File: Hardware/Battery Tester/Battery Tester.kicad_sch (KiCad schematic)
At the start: 16 parts, among them J1 USB4105-GF-A, J2 Conn_01x02_Socket, SW1 SW_SPST, U1 MCP73831-5-OT, U2 LP5907MFX-3.3_NOPB

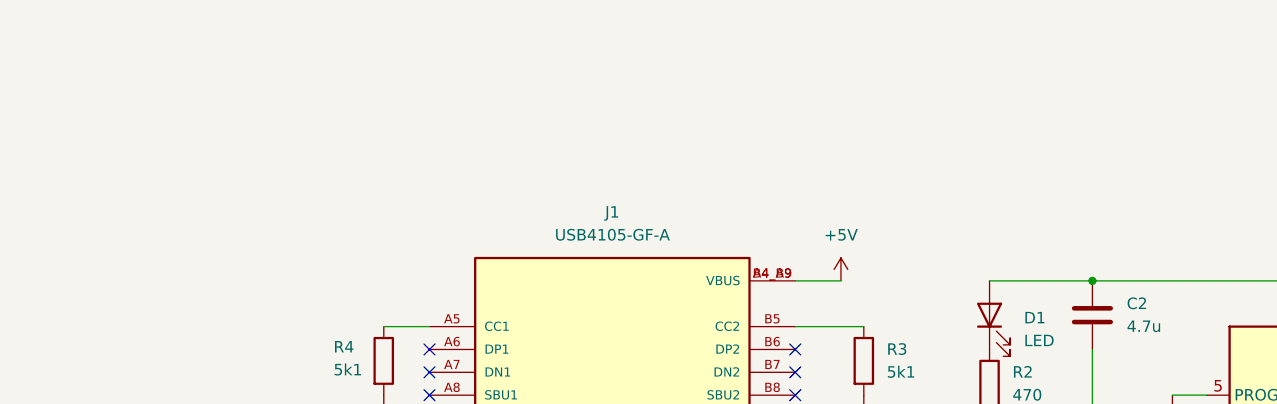
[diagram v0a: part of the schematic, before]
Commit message: Adding PDFs for the schematics
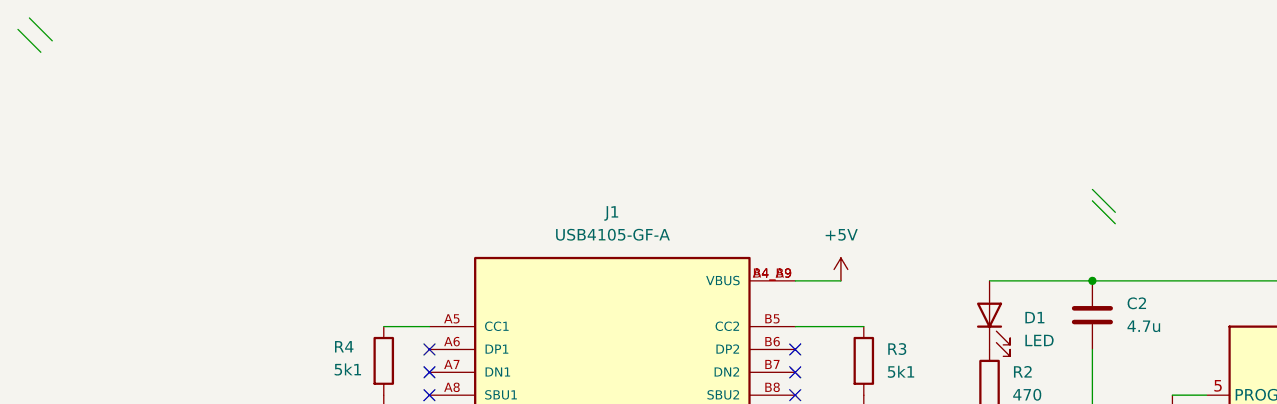
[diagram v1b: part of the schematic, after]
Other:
- title: (none) -> Battery Tester
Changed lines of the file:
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@@
 	(generator_version "8.0")
 	(paper "A4")
+	(title_block
+		(title "Battery Tester")
+		(date "2024-04-16")
+		(rev "Rev A")
+	)
 	(junction
 		(at 241.3 45.72)
@@
 		(at 29.21 43.18)
 	)
+	(bus_entry
+		(at -16.51 2.54)
+		(size 2.54 2.54)
+		(stroke
+			(width 0)
+			(type default)
+		)
+	)
+	(bus_entry
+		(at -15.24 1.27)
+		(size 2.54 2.54)
+		(stroke
+			(width 0)
+			(type default)
+		)
+	)
+	(bus_entry
+		(at 102.87 21.59)
+		(size 2.54 2.54)
+		(stroke
+			(width 0)
+			(type default)
+		)
+	)
+	(bus_entry
+		(at 102.87 20.32)
+		(size 2.54 2.54)
+		(stroke
+			(width 0)
+			(type default)
+		)
+	)
 	(wire
